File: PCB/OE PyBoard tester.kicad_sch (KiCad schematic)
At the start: 51 parts, among them J1 6pin_hd, J4 3pin_hd, J5 USB4105-GF-A, SW1 SW_SPST, U4 ATXMEGA32A4U-MH, U7 FT232RNL, U8 LP5907MFX-3.3

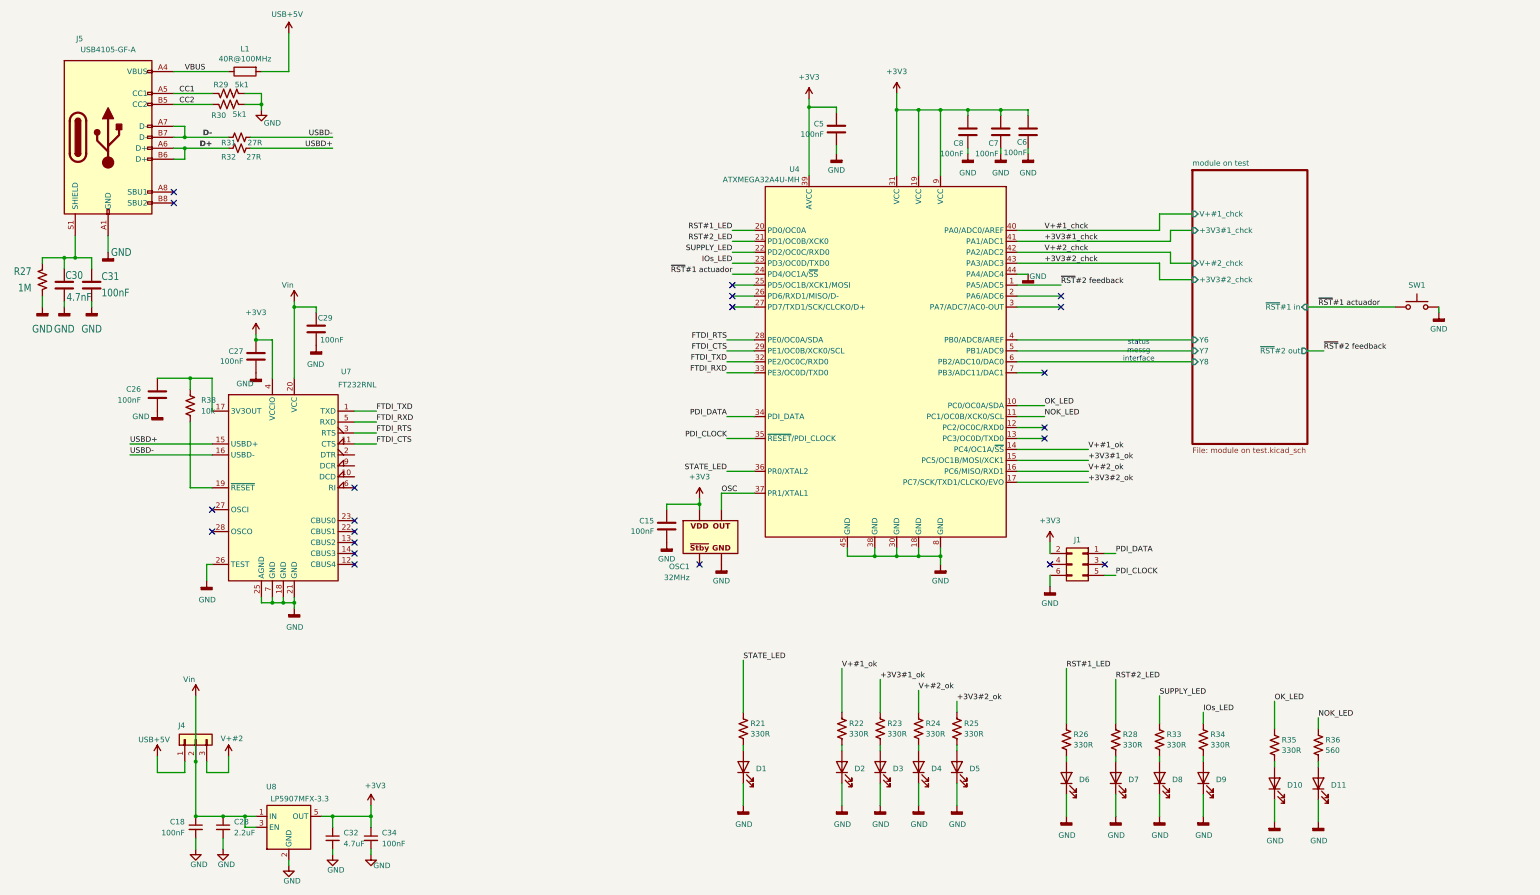
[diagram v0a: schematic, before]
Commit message: modificado nome projecto - OE PyBoard tester
OE PyBoard tester
- feita nova anotação para componentes ficarem com Referências sem jumps
- novo nome às Symbol & Footprint Libraries
- optimizadas link de componentes & footprints às novas Libraries
- retirado campo 'values' de Fab. Layer
- gerados novos ficheiros de produção: Gerbers & Drills & P&P & .d356 & BOM
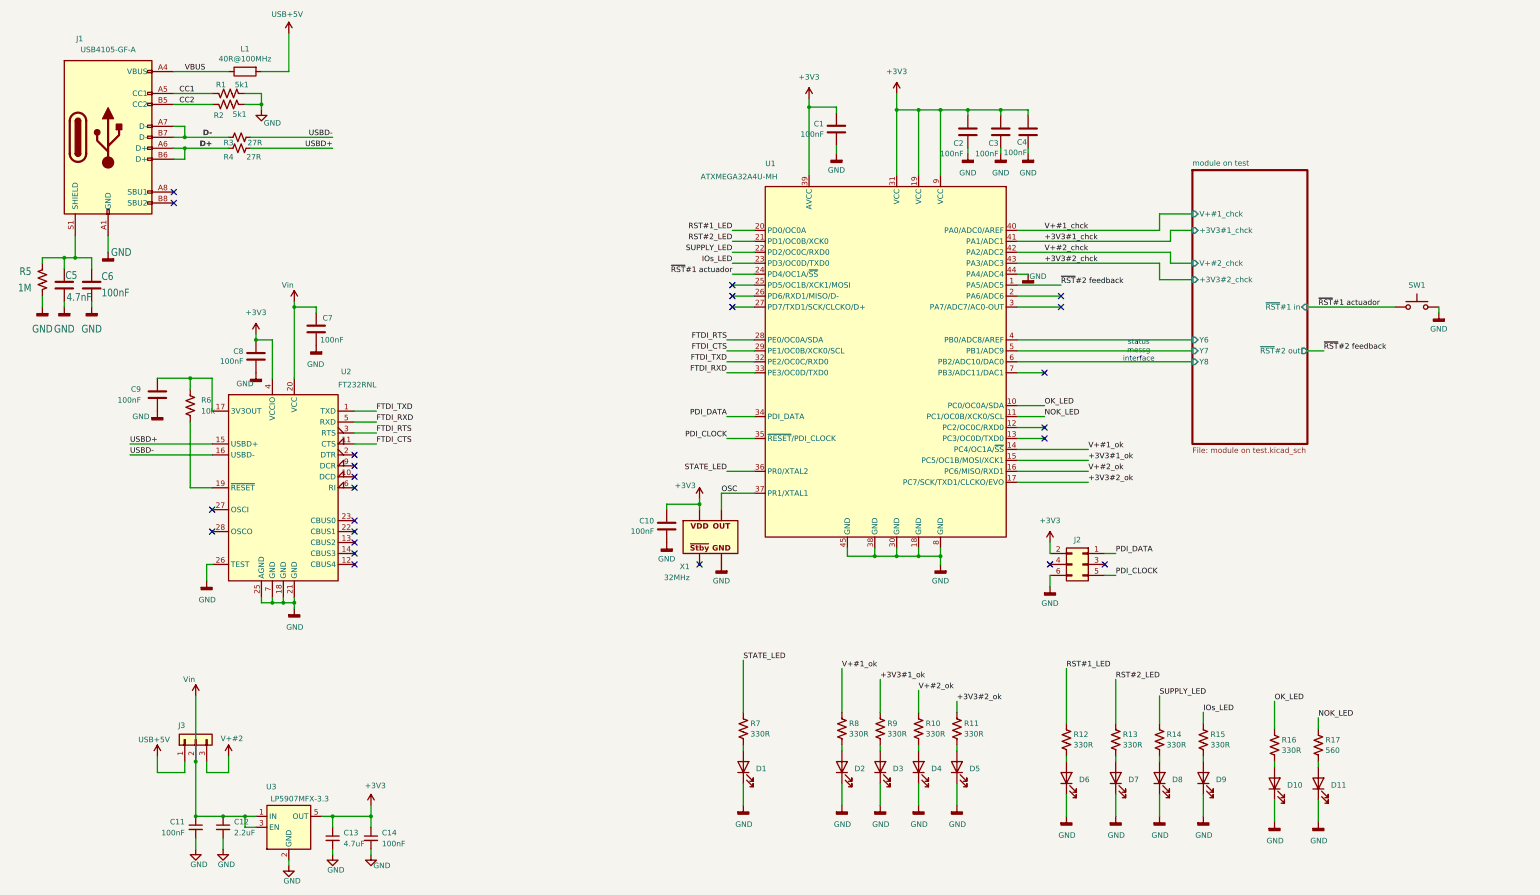
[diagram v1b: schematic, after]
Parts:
- C1: renamed from C5; ASSEMBLY Yes -> (none)
- C10: renamed from C15; ASSEMBLY Yes -> (none)
- C2: renamed from C8; ASSEMBLY Yes -> (none)
- C3: renamed from C7; ASSEMBLY Yes -> (none)
- C4: renamed from C6; ASSEMBLY Yes -> (none)
- J1: renamed from J5; footprint Connector_USB:USB_C_Receptacle_GCT_USB4105-xx-A_16P_TopMnt_Horizontal -> PyBoardTester FootprintLib:USB_C_Receptacle_GCT_USB4105-xx-A_16P_TopMnt_Horizontal
- J2: renamed from J1; ASSEMBLY Yes -> (none)
- J3: renamed from J4; MPN 2212S-03SG-85 -> n.a.; OEPSPN OEPS070137 -> OEPS000000
- R10: renamed from R24; ASSEMBLY Yes -> (none)
- R11: renamed from R25; ASSEMBLY Yes -> (none)
- R12: renamed from R26; ASSEMBLY Yes -> (none)
- R13: renamed from R28; ASSEMBLY Yes -> (none)
- R14: renamed from R33; ASSEMBLY Yes -> (none)
- R15: renamed from R34; ASSEMBLY Yes -> (none)
- R16: renamed from R35; ASSEMBLY Yes -> (none)
- R17: renamed from R36; ASSEMBLY Yes -> (none)
- R6: renamed from R38; ASSEMBLY Yes -> (none)
- R7: renamed from R21; ASSEMBLY Yes -> (none)
- R8: renamed from R22; ASSEMBLY Yes -> (none)
- R9: renamed from R23; ASSEMBLY Yes -> (none)
- U1: renamed from U4; symbol _symbolLib:ATXMEGA32A4U -> PyBoardTester:ATXMEGA32A4U; ASSEMBLY Yes -> (none)
- U2: renamed from U7; symbol _symbolLib:FT232RL -> PyBoardTester:FT232RL
- X1: renamed from OSC1; footprint _footprintLib:OSC -> PyBoardTester FootprintLib:OSC; symbol _symbolLib:OSC_1 -> PyBoardTester:OSCILLATOR; ASSEMBLY Yes -> (none)
- renumbered C18 to C11, C28 to C12, C32 to C13, C34 to C14, C30 to C5, C31 to C6, C29 to C7, C27 to C8, C26 to C9, R29 to R1, R30 to R2, R31 to R3, R32 to R4, R27 to R5, U8 to U3
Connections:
- no-connect marks 21 -> 24

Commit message: synchronizing with main branch
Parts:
- added NOK1, OK1: SW_SPST, Button_Switch_SMD:SW_SPST_TL3305B, symbol Switch:SW_Push
- R1, R2: value 5k1 -> 5k1 0.1%; MPN ERJ-2RKF5101X -> RT0402BRD075K1L; OEPSPN OEPS020173 -> OEPS020203
- R6: value 10k -> 10k 0.1%
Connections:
- net GND: now also NOK1.2, OK1.2
- net at U1.12 (PC2/OC0C/RXD0): now also OK1.1
- net at U1.13 (PC3/OC0D/TXD0): now also NOK1.1
- no-connect marks 24 -> 22
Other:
- moved on the sheet: SW1
